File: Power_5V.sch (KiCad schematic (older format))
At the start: 7 parts

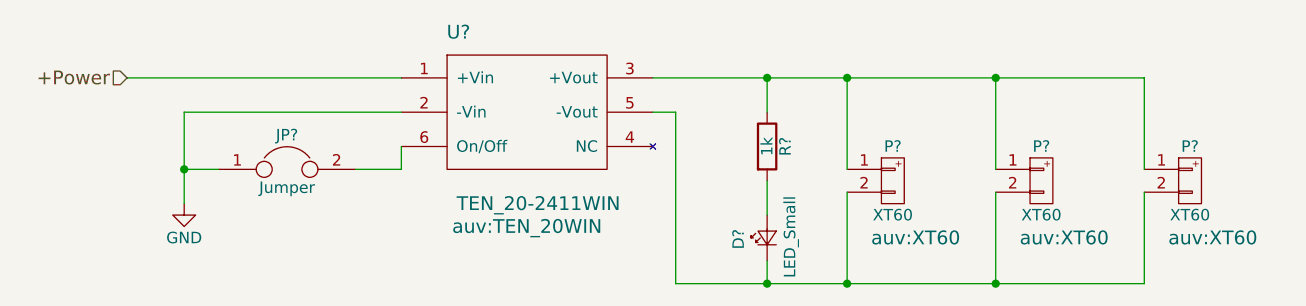
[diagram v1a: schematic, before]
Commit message: Correct all foot-print assignments
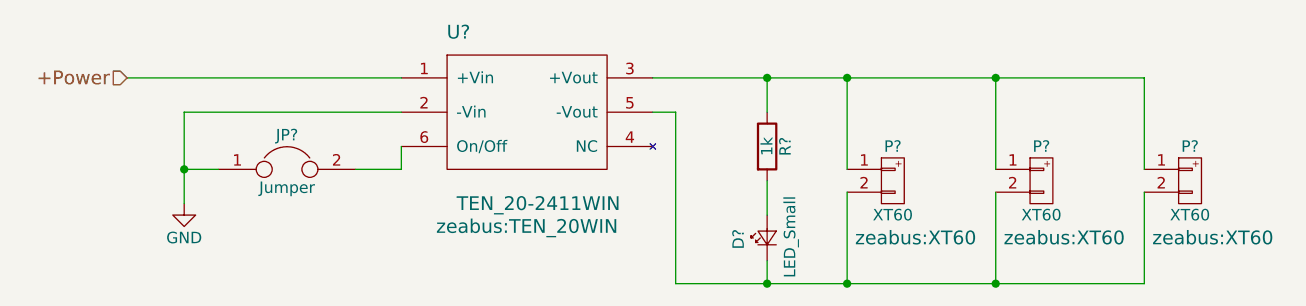
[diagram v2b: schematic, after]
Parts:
- P? (x3): footprint auv:XT60 -> zeabus:XT60
- U?: footprint auv:TEN_20WIN -> zeabus:TEN_20WIN
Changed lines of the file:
@@
 $Descr A4 11693 8268
 encoding utf-8
-Sheet 2 12
+Sheet 2 13
 Title ""
 Date ""
@@
 F 0 "U?" H 5250 3650 60  0000 C CNN
 F 1 "TEN_20-2411WIN" H 5600 2900 60  0000 C CNN
-F 2 "auv:TEN_20WIN" H 5550 2800 60  0000 C CNN
+F 2 "zeabus:TEN_20WIN" H 5550 2800 60  0000 C CNN
 F 3 "" H 5600 3200 60  0000 C CNN
 	1    5550 3300
@@
 F 0 "P?" H 7150 3750 50  0000 C CNN
 F 1 "XT60" H 7150 3450 50  0000 C CNN
-F 2 "auv:XT60" H 7250 3350 60  0000 C CNN
+F 2 "zeabus:XT60" H 7250 3350 60  0000 C CNN
 F 3 "" H 7150 3600 60  0000 C CNN
 	1    7150 3600
@@
 F 0 "P?" H 7800 3750 50  0000 C CNN
 F 1 "XT60" H 7800 3450 50  0000 C CNN
-F 2 "auv:XT60" H 7900 3350 60  0000 C CNN
+F 2 "zeabus:XT60" H 7900 3350 60  0000 C CNN
 F 3 "" H 7800 3600 60  0000 C CNN
 	1    7800 3600
@@
 F 0 "P?" H 8450 3750 50  0000 C CNN
 F 1 "XT60" H 8450 3450 50  0000 C CNN
-F 2 "auv:XT60" H 8550 3350 60  0000 C CNN
+F 2 "zeabus:XT60" H 8550 3350 60  0000 C CNN
 F 3 "" H 8450 3600 60  0000 C CNN
 	1    8450 3600

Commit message: Annotate all components
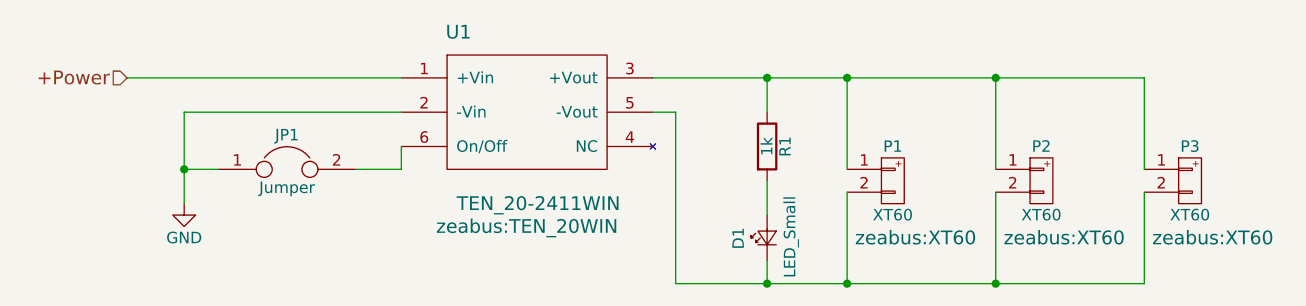
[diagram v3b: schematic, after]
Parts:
- gave numbers to parts that had none: 7
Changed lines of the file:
@@
 LIBS:zeabus
 LIBS:ftdi
-LIBS:Power_Distributor-cache
 EELAYER 25 0
 EELAYER END
@@
 $EndDescr
 $Comp
-L TEN_20-2411WIN U?
+L TEN_20-2411WIN U1
 U 1 1 58C99133
 P 5550 3300
-F 0 "U?" H 5250 3650 60  0000 C CNN
+F 0 "U1" H 5250 3650 60  0000 C CNN
 F 1 "TEN_20-2411WIN" H 5600 2900 60  0000 C CNN
 F 2 "zeabus:TEN_20WIN" H 5550 2800 60  0000 C CNN
@@
 $EndComp
 $Comp
-L LED_Small D?
+L LED_Small D1
 U 1 1 58C99171
 P 6600 3850
-F 0 "D?" H 6550 3975 50  0000 L CNN
+F 0 "D1" H 6550 3975 50  0000 L CNN
 F 1 "LED_Small" H 6425 3750 50  0000 L CNN
 F 2 "LEDs:LED_0603" V 6600 3850 50  0001 C CNN
@@
 $EndComp
 $Comp
-L R R?
+L R R1
 U 1 1 58C991CE
 P 6600 3450
-F 0 "R?" V 6680 3450 50  0000 C CNN
+F 0 "R1" V 6680 3450 50  0000 C CNN
 F 1 "1k" V 6600 3450 50  0000 C CNN
 F 2 "Resistors_SMD:R_0603" V 6530 3450 50  0001 C CNN
@@
 $EndComp
 $Comp
-L GND #PWR?
+L GND #PWR013
 U 1 1 58C991F7
 P 4050 3700
-F 0 "#PWR?" H 4050 3450 50  0001 C CNN
+F 0 "#PWR013" H 4050 3450 50  0001 C CNN
 F 1 "GND" H 4050 3550 50  0000 C CNN
 F 2 "" H 4050 3700 50  0001 C CNN
@@
 $EndComp
 $Comp
-L Jumper JP?
+L Jumper JP1
 U 1 1 58C99211
 P 4500 3550
-F 0 "JP?" H 4500 3700 50  0000 C CNN
+F 0 "JP1" H 4500 3700 50  0000 C CNN
 F 1 "Jumper" H 4500 3470 50  0000 C CNN
 F 2 "Pin_Headers:Pin_Header_Straight_1x02_Pitch2.00mm" H 4500 3550 50  0001 C CNN
@@
 	3800 3150 5000 3150
 $Comp
-L XT60 P?
+L XT60 P1
 U 1 1 58C9F835
 P 7150 3600
-F 0 "P?" H 7150 3750 50  0000 C CNN
+F 0 "P1" H 7150 3750 50  0000 C CNN
 F 1 "XT60" H 7150 3450 50  0000 C CNN
 F 2 "zeabus:XT60" H 7250 3350 60  0000 C CNN
@@
 $EndComp
 $Comp
-L XT60 P?
+L XT60 P2
 U 1 1 58DFD635
 P 7800 3600
-F 0 "P?" H 7800 3750 50  0000 C CNN
+F 0 "P2" H 7800 3750 50  0000 C CNN
 F 1 "XT60" H 7800 3450 50  0000 C CNN
 F 2 "zeabus:XT60" H 7900 3350 60  0000 C CNN
@@
 Connection ~ 6950 4050
 $Comp
-L XT60 P?
+L XT60 P3
 U 1 1 58DFD6BF
 P 8450 3600
-F 0 "P?" H 8450 3750 50  0000 C CNN
+F 0 "P3" H 8450 3750 50  0000 C CNN
 F 1 "XT60" H 8450 3450 50  0000 C CNN
 F 2 "zeabus:XT60" H 8550 3350 60  0000 C CNN
